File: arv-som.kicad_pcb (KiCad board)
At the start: 2 copper layers, 55 x 40 mm, 11 parts, among them J3 DF40C-100DP-0.4V(51), J4 DF40C-100DP-0.4V(51), U1 MT53E256M32D2DS-053, U10 TDA19988BHN_C1,557, U11 KSZ9031RNXCA, U12 MT53E256M32D2DS-053, U13 VIC7100, U8 TPS65086100, U9 GD25LQ256DWIGR

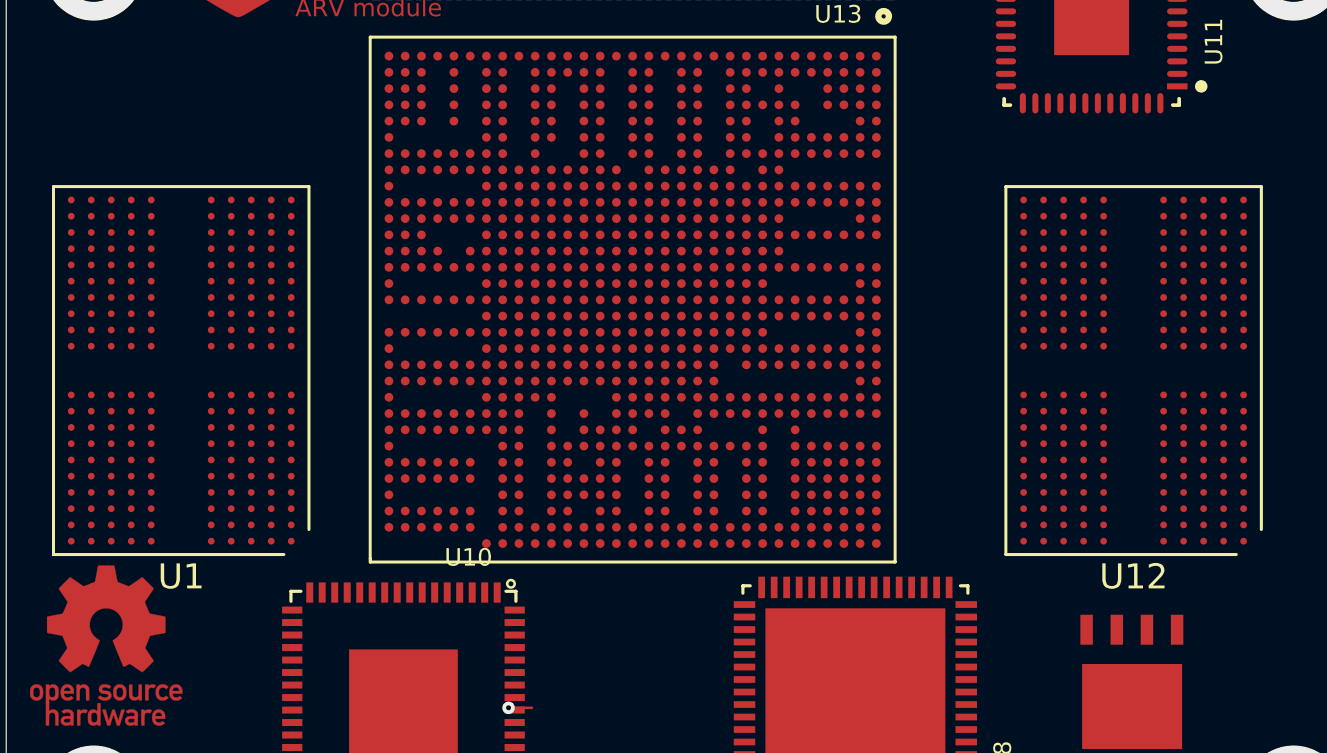
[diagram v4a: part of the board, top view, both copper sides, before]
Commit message: Schematic cleanup, added logotypes
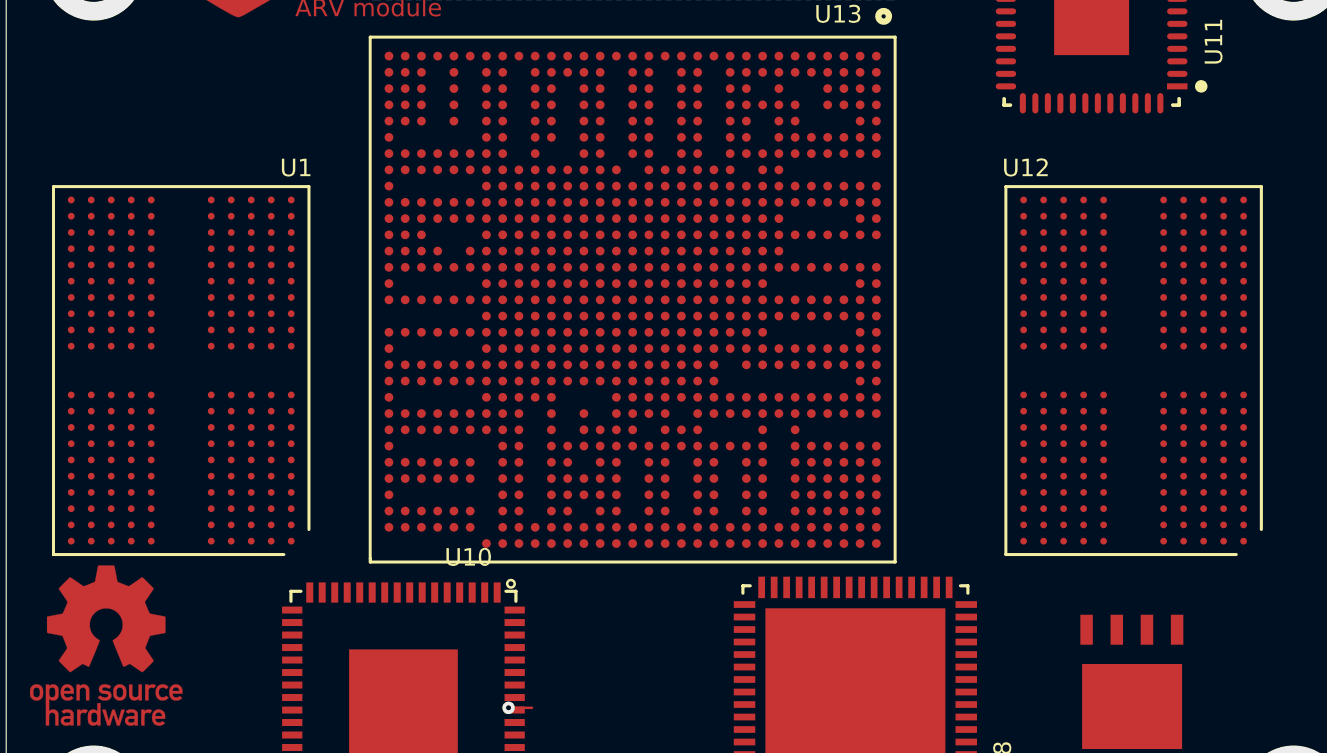
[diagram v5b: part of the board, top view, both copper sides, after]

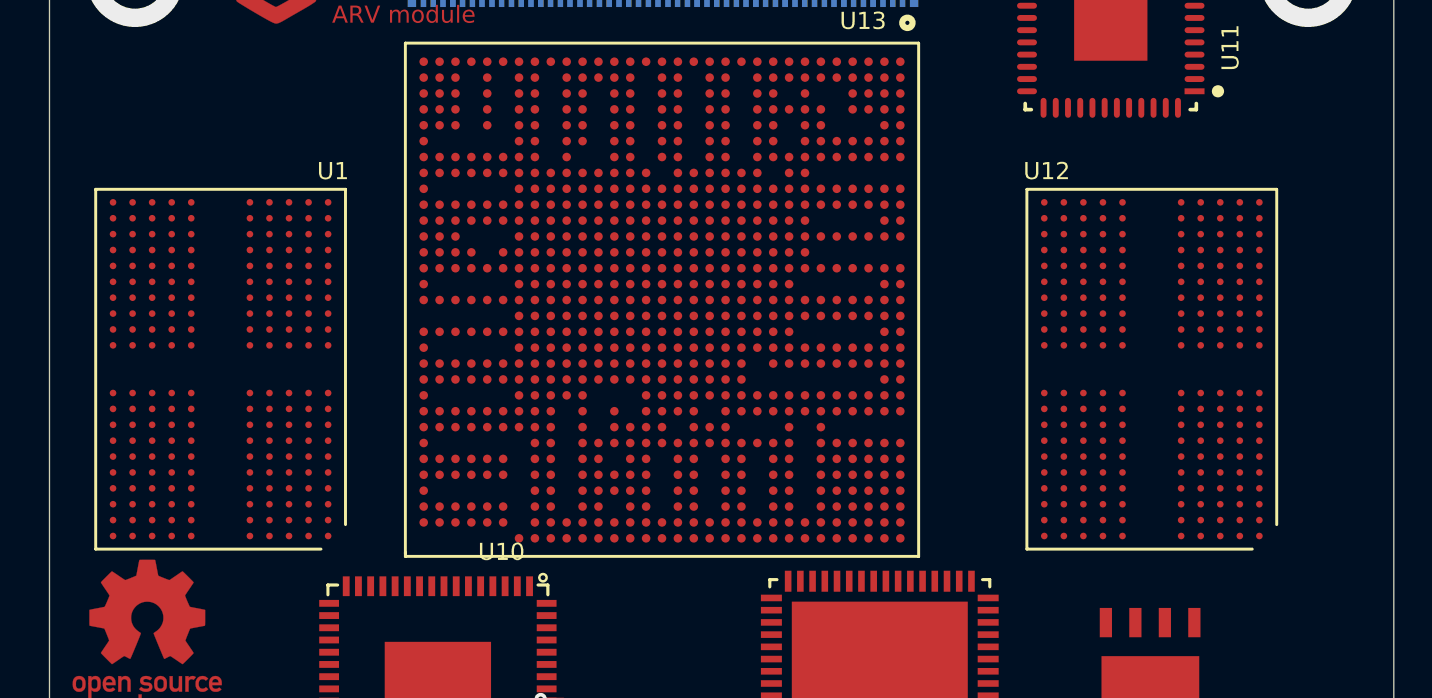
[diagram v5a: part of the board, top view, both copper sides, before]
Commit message: Added local libraries
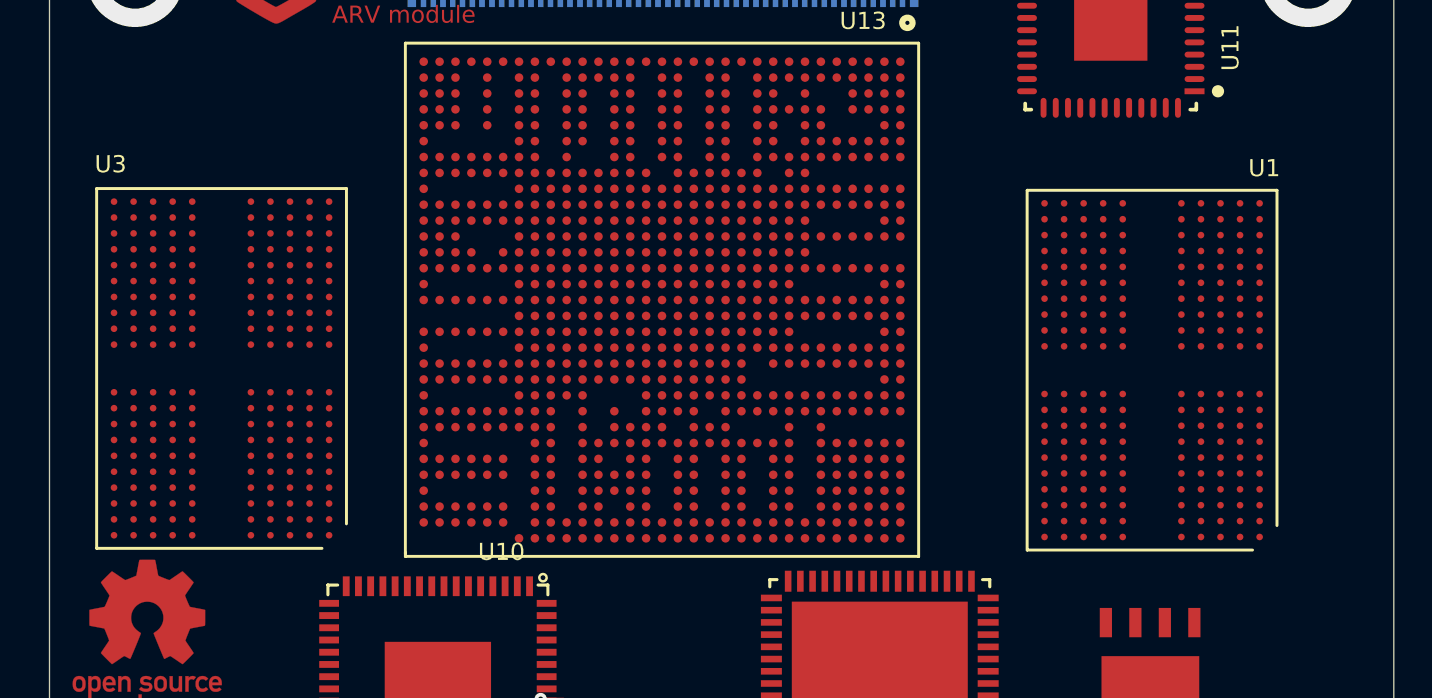
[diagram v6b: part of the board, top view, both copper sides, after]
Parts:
- removed U12: MT53E256M32D2DS-053, antmicro-footprints:BGA-200_10.0x14.5mm_Layout12x22_P0.80x0.65mm
- added U3: MT53D1024M32D4DT-053, antmicro-footprints:BGA-200_10.0x14.5mm_Layout12x22_P0.80x0.65mm, F.Cu at (137.1, 74.4)
- U1: value MT53E256M32D2DS-053 -> MT53D1024M32D4DT-053
- moved U1 38.1 mm to (175.1, 74.5)
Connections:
- net ATEMP_TEST0 renamed /VIC7100 config/ATEMP_TEST0
- net ATEMP_TEST1 renamed /VIC7100 config/ATEMP_TEST1
- net ATEMP_VCAL renamed /VIC7100 config/ATEMP_VCAL
- net ATEMP_VSS renamed /VIC7100 config/ATEMP_VSS
- net BT_RSTN renamed Net-(U13-PadN1)
- net BT_UART_CTS renamed Net-(U13-PadN2)
- net BT_UART_RTS renamed Net-(U13-PadR6)
- net BT_UART_RXD renamed Net-(U13-PadN4)
- net BT_UART_TXD renamed Net-(U13-PadR7)
- net BT_WAKE renamed Net-(U13-PadM5)
- net DAC_PWML renamed Net-(U13-PadV2)
- net DAC_PWMR renamed Net-(U13-PadV6)
- net Net-(J3-Pad16) renamed SYNC_IN
- net Net-(J3-Pad18) renamed SYNC_OUT
- net USB_SSRXA1 renamed Net-(U13-PadAD27)
- net USB_SSRXA2 renamed Net-(U13-PadAC31)
- net USB_SSRXB1 renamed Net-(U13-PadAD26)
- net USB_SSRXB2 renamed Net-(U13-PadAC30)
- net USB_SSTXA1 renamed Net-(U13-PadAC27)
- net USB_SSTXA2 renamed Net-(U13-PadAD30)
- net USB_SSTXB1 renamed Net-(U13-PadAC26)
- net USB_SSTXB2 renamed Net-(U13-PadAD31)
- net WIFI_EN renamed Net-(U13-PadP1)
- net WIFI_SDIO1_CLK renamed Net-(U13-PadN7)
- net WIFI_SDIO1_CMD renamed Net-(U13-PadM7)
- net WIFI_SDIO1_D0 renamed Net-(U13-PadN6)
- net WIFI_SDIO1_D1 renamed Net-(U13-PadM4)
- net WIFI_SDIO1_D2 renamed Net-(U13-PadM2)
- net WIFI_SDIO1_D3 renamed Net-(U13-PadM3)
- J3 pad 19: Net-(J3-Pad19) -> ETH_LED1
- J3 pad 21: PI_nLED_ACT -> LED
- J3 pad 70: SD_DAT2 -> SD_DAT7
- J3 pad 72: SD_DAT7 -> SD_DAT6
- J3 pad 80: I2C0_SCL -> I2C2_SCL
- J3 pad 82: I2C0_SDA -> I2C2_SDA
- J3 pad 84: 3V3_OUT -> VCC_3V3
- J3 pad 86: 3V3_OUT -> VCC_3V3
- J3 pad 88: 1V8_OUT -> VCC_1V8
- J3 pad 90: 1V8_OUT -> VCC_1V8
- J3 pad 92: RUN_PG -> CTL5
- J3 pad 97: CAM_GPIO -> CSI0_PWDN
- J4 pad 57: CDTX_DSI_D0_N -> DSI1_D0_N
- J4 pad 59: CDTX_DSI_D0_P -> DSI1_D0_P
- J4 pad 63: CDTX_DSI_D1_N -> DSI1_D1_N
- J4 pad 65: CDTX_DSI_D1_P -> DSI1_D1_P
- J4 pad 69: CDTX_DSI_D2_N -> DSI0_C_N
- J4 pad 71: CDTX_DSI_D2_P -> DSI0_C_P
- J4 pad 75: DSI1_D0_N -> CDTX_DSI_D0_N
- J4 pad 77: DSI1_D0_P -> CDTX_DSI_D0_P
- J4 pad 81: DSI1_D1_N -> CDTX_DSI_D1_N
- J4 pad 83: DSI1_D1_P -> CDTX_DSI_D1_P
- J4 pad 87: DSI1_C_N -> CDTX_DSI_D2_N
- J4 pad 89: DSI1_C_P -> CDTX_DSI_D2_P
- J4 pad 93: DSI2_D1_N -> CDTX_DSI_D3_N
- J4 pad 94: DSI1_D3_N -> CDTX_DSI_D4_N
- J4 pad 95: DSI2_D1_P -> CDTX_DSI_D3_P
- J4 pad 96: DSI1_D3_P -> CDTX_DSI_D4_P
- U1 pad AA11: DDR1_DQ24 -> DDR0_DQ24
- U1 pad AA2: DDR1_DQ16 -> DDR0_DQ16
- U1 pad AA4: DDR1_DQ23 -> DDR0_DQ23
- U1 pad AA9: DDR1_DQ31 -> DDR0_DQ31
- U1 pad B11: DDR1_DQ08 -> DDR0_DQ08
- U1 pad B2: DDR1_DQ00 -> DDR0_DQ00
- U1 pad B4: DDR1_DQ07 -> DDR0_DQ07
- U1 pad B9: DDR1_DQ15 -> DDR0_DQ15
- U1 pad C10: DDR1_DMI1 -> DDR0_DMI1
- U1 pad C11: DDR1_DQ09 -> DDR0_DQ09
- U1 pad C2: DDR1_DQ01 -> DDR0_DQ01
- U1 pad C3: DDR1_DMI0 -> DDR0_DMI0
- U1 pad C4: DDR1_DQ06 -> DDR0_DQ06
- U1 pad C9: DDR1_DQ14 -> DDR0_DQ14
- U1 pad D10: DDR1_DQS1N -> DDR0_DQS1N
- U1 pad D3: DDR1_DQS0N -> DDR0_DQS0N
- U1 pad E10: DDR1_DQS1P -> DDR0_DQS1P
- U1 pad E11: DDR1_DQ10 -> DDR0_DQ10
- U1 pad E2: DDR1_DQ02 -> DDR0_DQ02
- U1 pad E3: DDR1_DQS0P -> DDR0_DQS0P
- U1 pad E4: DDR1_DQ05 -> DDR0_DQ05
- U1 pad E9: DDR1_DQ13 -> DDR0_DQ13
- U1 pad F11: DDR1_DQ11 -> DDR0_DQ11
- U1 pad F2: DDR1_DQ03 -> DDR0_DQ03
- U1 pad F4: DDR1_DQ04 -> DDR0_DQ04
- U1 pad F9: DDR1_DQ12 -> DDR0_DQ12
- U1 pad H10: DDR1_A03 -> DDR0_A03
- U1 pad H11: DDR1_A04 -> DDR0_A04
- U1 pad H2: DDR1_A00 -> DDR0_A00
- U1 pad H3: DDR1_CS1 -> DDR0_CS1
- U1 pad H4: DDR1_CS0 -> DDR0_CS0
- U1 pad H9: DDR1_A02 -> DDR0_A02
- U1 pad J11: DDR1_A05 -> DDR0_A05
- U1 pad J2: DDR1_A01 -> DDR0_A01
- U1 pad J4: DDR1_CKE0 -> DDR0_CKE0
- U1 pad J5: DDR1_CKE1 -> DDR0_CKE1
- U1 pad J8: DDR1_CK0_N -> DDR0_CK0_N
- U1 pad J9: DDR1_CK0_P -> DDR0_CK0_P
- U1 pad P11: DDR1_A05 -> DDR0_A05
- U1 pad P2: DDR1_A01 -> DDR0_A01
- U1 pad P4: DDR1_CKE0 -> DDR0_CKE0
- U1 pad P5: DDR1_CKE1 -> DDR0_CKE1
- U1 pad P8: DDR1_CK1_N -> DDR0_CK1_N
- U1 pad P9: DDR1_CK1_P -> DDR0_CK1_P
- U1 pad R10: DDR1_A03 -> DDR0_A03
- U1 pad R11: DDR1_A04 -> DDR0_A04
- U1 pad R2: DDR1_A00 -> DDR0_A00
- U1 pad R3: DDR_CS3 -> DDR0_CS3
- U1 pad R4: DDR1_CS2 -> DDR0_CS2
- U1 pad R9: DDR1_A02 -> DDR0_A02
- U1 pad T2: DDR1_ODT_1 -> DDR0_ODT_1
- U1 pad U11: DDR1_DQ27 -> DDR0_DQ27
- U1 pad U2: DDR1_DQ19 -> DDR0_DQ19
- U1 pad U4: DDR1_DQ20 -> DDR0_DQ20
- U1 pad U9: DDR1_DQ28 -> DDR0_DQ28
- U1 pad V10: DDR1_DQS3P -> DDR0_DQS3P
- U1 pad V11: DDR1_DQ26 -> DDR0_DQ26
- U1 pad V2: DDR1_DQ18 -> DDR0_DQ18
- U1 pad V3: DDR1_DQS2P -> DDR0_DQS2P
- U1 pad V4: DDR1_DQ21 -> DDR0_DQ21
- U1 pad V9: DDR1_DQ29 -> DDR0_DQ29
- U1 pad W10: DDR1_DQS3N -> DDR0_DQS3N
- U1 pad W3: DDR1_DQS2N -> DDR0_DQS2N
- U1 pad Y10: DDR1_DMI3 -> DDR0_DMI3
- U1 pad Y11: DDR1_DQ25 -> DDR0_DQ25
- U1 pad Y2: DDR1_DQ17 -> DDR0_DQ17
- U1 pad Y3: DDR1_DMI2 -> DDR0_DMI2
- U1 pad Y4: DDR1_DQ22 -> DDR0_DQ22
- U1 pad Y9: DDR1_DQ30 -> DDR0_DQ30
- U13 pad AA1: LCD_VSYNC -> Net-(R62-Pad2)
- U13 pad AA2: LCD_DATA3 -> Net-(R67-Pad2)
- U13 pad AA3: LCD_PCLK -> Net-(R60-Pad2)
- U13 pad AA4: LCD_DE -> Net-(R61-Pad2)
- U13 pad AA5: LCD_DATA0 -> Net-(R64-Pad2)
- U13 pad AA6: LCD_DATA1 -> Net-(R65-Pad2)
- U13 pad AB1: LCD_DATA2 -> Net-(R66-Pad2)
- U13 pad AB2: LCD_DATA7 -> Net-(R71-Pad2)
- U13 pad AB4: LCD_DATA11 -> Net-(R75-Pad2)
- U13 pad AB5: LCD_DATA4 -> Net-(R68-Pad2)
- U13 pad AB6: LCD_DATA5 -> Net-(R69-Pad2)
- U13 pad AB7: LCD_DATA8 -> Net-(R72-Pad2)
- U13 pad AC1: LCD_DATA6 -> Net-(R70-Pad2)
- U13 pad AD1: LCD_DATA10 -> Net-(R74-Pad2)
- U13 pad AD2: LCD_DATA15 -> Net-(R79-Pad2)
- U13 pad AD3: LCD_DATA18 -> Net-(R82-Pad2)
- U13 pad AD4: LCD_DATA22 -> Net-(R86-Pad2)
- U13 pad AD5: LCD_DATA23 -> Net-(R87-Pad2)
- U13 pad AE1: LCD_DATA14 -> Net-(R78-Pad2)
- U13 pad AE2: LCD_DATA19 -> Net-(R83-Pad2)
- U13 pad AE4: LCD_DATA20 -> Net-(R84-Pad2)
- U13 pad AG2: LCD_DATA9 -> Net-(R73-Pad2)
- U13 pad AG3: LCD_DATA13 -> Net-(R77-Pad2)
- U13 pad AG4: LCD_DATA17 -> Net-(R81-Pad2)
- U13 pad AL3: LCD_DATA16 -> Net-(R80-Pad2)
- U13 pad Y2: LCD_HSYNC -> Net-(R63-Pad2)
- U8 pad 11: Net-(C2-Pad2) -> VCC_5V0
- U8 pad 21: LDO_3V3 -> VCC_5V0
- U8 pad 24: Net-(C2-Pad2) -> VCC_5V0
- U8 pad 31: Net-(C10-Pad2) -> VDD2PEN_OTP_1V8
- U8 pad 38: Net-(C2-Pad2) -> VCC_5V0
- U8 pad 8: Net-(C2-Pad2) -> VCC_5V0
- U8 pad 9: VDD2PEN_OTP_1V8 -> LDO_3V3

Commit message: Update libraries
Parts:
- J3, J4: footprint antmicro-footprints:HRS_DF40C-100DP-0.4V(51) -> arv-som-footprints:HRS_DF40C-100DP-0.4V(51)
- N1: footprint antmicro-footprints:antmicro-logo_scaled_12mm -> arv-som-footprints:antmicro-logo_scaled_12mm
- N2: footprint antmicro-footprints:oshw-logo -> arv-som-footprints:oshw-logo
- U1, U3: footprint antmicro-footprints:BGA-200_10.0x14.5mm_Layout12x22_P0.80x0.65mm -> arv-som-footprints:BGA-200_10.0x14.5mm_Layout12x22_P0.80x0.65mm
- U10: footprint antmicro-footprints:QFN50P900X900X100-65N -> arv-som-footprints:QFN50P900X900X100-65N
- U11: footprint antmicro-footprints:QFN-48-Microchip-QFN77-48LD-PL-2 -> arv-som-footprints:QFN-48-Microchip-QFN77-48LD-PL-2
- U13: footprint antmicro-footprints:vic7100 -> arv-som-footprints:vic7100
- U8: footprint antmicro-footprints:QFN50P900X900X80-65N -> arv-som-footprints:QFN50P900X900X80-65N
- U9: footprint antmicro-footprints:8-WSON-6x5 -> arv-som-footprints:8-WSON-6x5
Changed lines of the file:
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@@
     (add_net nRPIBOOT)
   )
-  (module antmicro-footprints:BGA-200_10.0x14.5mm_Layout12x22_P0.80x0.65mm (layer F.Cu)
+  (module arv-som-footprints:BGA-200_10.0x14.5mm_Layout12x22_P0.80x0.65mm (layer F.Cu)
     (at 137.06 74.44 180)
     (descr "BGA-200, 14.5x10.0mm, 200 Ball, 12x22 Layout, 0.8x0.65mm Pitch, http://www.issi.com/WW/pdf/43-46LQ32256A-AL.pdf")
@@
     )
   )
-  (module antmicro-footprints:BGA-200_10.0x14.5mm_Layout12x22_P0.80x0.65mm (layer F.Cu)
+  (module arv-som-footprints:BGA-200_10.0x14.5mm_Layout12x22_P0.80x0.65mm (layer F.Cu)
     (at 175.13 74.51 180)
     (descr "BGA-200, 14.5x10.0mm, 200 Ball, 12x22 Layout, 0.8x0.65mm Pitch, http://www.issi.com/WW/pdf/43-46LQ32256A-AL.pdf")
@@
     )
   )
-  (module antmicro-footprints:oshw-logo (layer F.Cu)
+  (module arv-som-footprints:oshw-logo (layer F.Cu)
     (at 134.02 85.47)
     (attr virtual)
@@
       (xy -1.520547 2.559315)) (layer F.Mask) (width 0.01))
   )
-  (module antmicro-footprints:antmicro-logo_scaled_12mm (layer F.Cu)
+  (module arv-som-footprints:antmicro-logo_scaled_12mm (layer F.Cu)
     (at 143.52 58.47)
     (attr virtual)
@@
     )
   )
-  (module antmicro-footprints:8-WSON-6x5 (layer F.Cu)
+  (module arv-som-footprints:8-WSON-6x5 (layer F.Cu)
     (at 172.520001 90.958002 90)
     (fp_text reference U9 (at 0.5 -1.1 270) (layer F.SilkS)
@@
     )
   )
-  (module antmicro-footprints:vic7100 (layer F.Cu)
+  (module arv-som-footprints:vic7100 (layer F.Cu)
     (at 164.830001 61.240002 270)
     (fp_text reference U13 (at -1.016 1.525) (layer F.SilkS)
@@
     )
   )
-  (module antmicro-footprints:QFN-48-Microchip-QFN77-48LD-PL-2 (layer F.Cu)
+  (module arv-som-footprints:QFN-48-Microchip-QFN77-48LD-PL-2 (layer F.Cu)
     (at 173.440001 60.350002 180)
     (fp_text reference U11 (at -4.9 0 90) (layer F.SilkS)
@@
     )
   )
-  (module antmicro-footprints:QFN50P900X900X100-65N (layer F.Cu)
+  (module arv-som-footprints:QFN50P900X900X100-65N (layer F.Cu)
     (at 145.910001 87.800002 270)
     (fp_text reference U10 (at -5.85 -2.6) (layer F.SilkS)
@@
     )
   )
-  (module antmicro-footprints:QFN50P900X900X80-65N (layer F.Cu)
+  (module arv-som-footprints:QFN50P900X900X80-65N (layer F.Cu)
     (at 163.990001 87.580002 180)
     (fp_text reference U8 (at -5.9 -2.35 90) (layer F.SilkS)
@@
     )
   )
-  (module "antmicro-footprints:HRS_DF40C-100DP-0.4V(51)" (layer B.Cu)
+  (module "arv-som-footprints:HRS_DF40C-100DP-0.4V(51)" (layer B.Cu)
     (at 155.120001 91.970002 180)
     (fp_text reference J4 (at -10.25 -2.5) (layer B.SilkS)
@@
     )
   )
-  (module "antmicro-footprints:HRS_DF40C-100DP-0.4V(51)" (layer B.Cu)
+  (module "arv-som-footprints:HRS_DF40C-100DP-0.4V(51)" (layer B.Cu)
     (at 155.120001 57.970002 180)
     (fp_text reference J3 (at 10 2.5) (layer B.SilkS)

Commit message: Added DDR layout (wip)
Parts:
- moved U11 11.0 mm to (177.4, 50.0)
- moved U1 4.78 mm to (175.4, 69.7)
- moved U3 2.37 mm to (139.2, 73.3)
- moved U13 2.21 mm to (167.0, 60.9)
- moved U8 0.88 mm to (164.1, 88.5)
- moved U10 0.88 mm to (146.0, 88.7)
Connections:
- U13 pad AJ5: (no net) -> DDR1_DQ31
- U3 pad AB4: VDD2 -> VDDQ
- U3 pad B10: VDDQ -> VDD2
- U3 pad B8: VDDQ -> VDD2
- U3 pad F5: VDD2 -> VDDQ
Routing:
- net GND: track 0.00 -> 408.6 mm, vias 0 -> 227
- net VCC_1V1: track 0.00 -> 71.9 mm, vias 0 -> 32
- net VCC_0V9: track 0.00 -> 60.5 mm, vias 0 -> 29
- net VDD2: track 0.00 -> 58.6 mm, vias 0 -> 41
- net VDDQ: track 0.00 -> 53.4 mm, vias 0 -> 40
- net VDD1: track 0.00 -> 37.1 mm, vias 0 -> 17
- net DDR1_A03: track 0.00 -> 31.2 mm, vias 0 -> 2
- net DDR1_A02: track 0.00 -> 31.0 mm, vias 0 -> 2
- net DDR1_A00: track 0.00 -> 30.2 mm, vias 0 -> 2
- net DDR1_A05: track 0.00 -> 29.9 mm, vias 0 -> 2
- net DDR1_A01: track 0.00 -> 29.9 mm, vias 0 -> 2
- net DDR0_A04: track 0.00 -> 29.8 mm, vias 0 -> 2
- net DDR1_CS2: track 0.00 -> 29.4 mm, vias 0 -> 2
- net DDR1_A04: track 0.00 -> 28.9 mm, vias 0 -> 2
- net VCC_3V3: track 0.00 -> 28.8 mm, vias 0 -> 7
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- added copper zone on B.Cu, net (none)
- added copper zone on In2.Cu, net (none)
- added copper zone on In4.Cu, net (none)
- added copper zone on In7.Cu, net (none)
- added copper zone on In9.Cu, net (none)
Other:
- copper layers 2 -> 12
